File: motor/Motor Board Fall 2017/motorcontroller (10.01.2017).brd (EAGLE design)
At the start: 76.2 x 50.8 mm, 45 parts, among them CON2 MOLEX_5566-2, U1 TEENSY_3.1_BASIC_2, U2 PCA9685PW, U6 TCAN1042HVDR, X1 OSTVN02A150

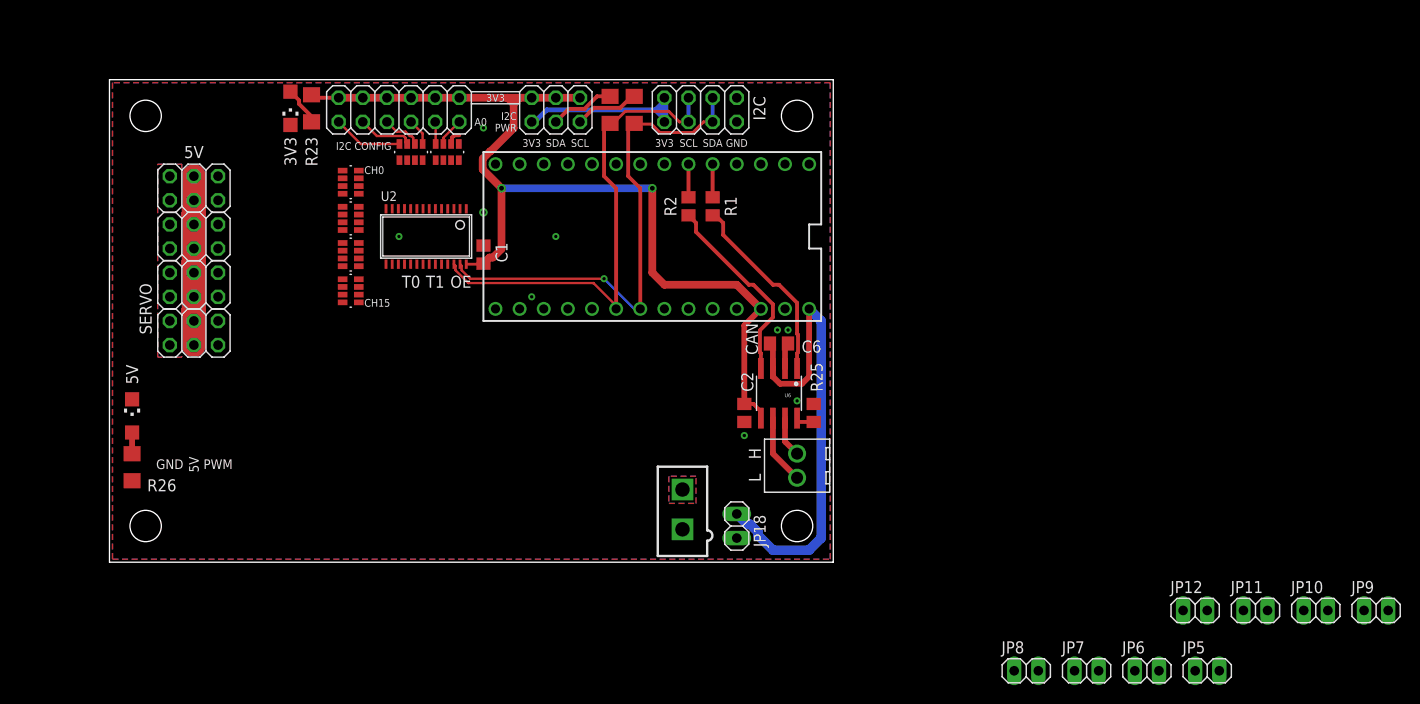
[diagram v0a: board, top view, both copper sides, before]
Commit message: Renamed labels
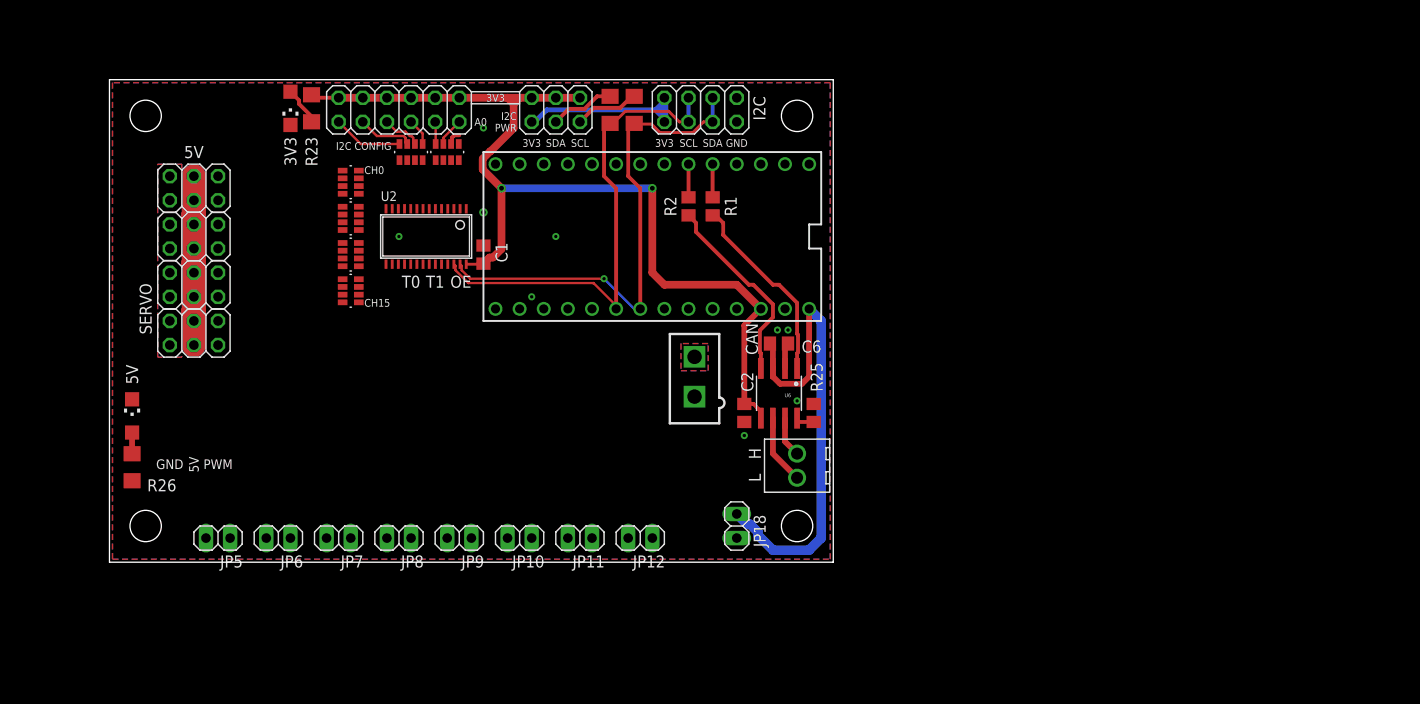
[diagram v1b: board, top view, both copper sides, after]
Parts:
- moved JP5 105.1 mm to (94.0, 74.9), turned to 180 degrees
- moved JP9 96.8 mm to (119.4, 74.9), turned to 180 degrees
- moved JP6 92.5 mm to (100.3, 74.9), turned to 180 degrees
- moved JP10 84.2 mm to (125.7, 74.9), turned to 180 degrees
- moved JP7 80.0 mm to (106.7, 74.9), turned to 180 degrees
- moved JP11 71.5 mm to (132.1, 74.9), turned to 180 degrees
- moved JP8 67.5 mm to (113.0, 74.9), turned to 180 degrees
- moved JP12 58.9 mm to (138.4, 74.9), turned to 180 degrees
- moved CON2 14.0 mm to (144.1, 91.9)
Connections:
- removed net LED_GATE0: R8.4
- removed net LED_GATE1: R8.3
- removed net LED_GATE2: R8.2
- removed net LED_GATE3: R8.1
- removed net PWM_SERVO10: R7.3
- removed net PWM_SERVO11: R7.4
- removed net PWM_SERVO8: R7.1
- removed net PWM_SERVO9: R7.2
- new net PWM_ESC0: R5.1
- new net PWM_ESC1: R5.2
- new net PWM_ESC2: R5.3
- new net PWM_ESC3: R5.4
- new net PWM_ESC4: R6.1
- new net PWM_ESC5: R6.2
- new net PWM_ESC6: R6.3
- new net PWM_ESC7: R6.4
- net PWM_SERVO0: now also R7.1; no longer R5.1
- net PWM_SERVO1: now also R7.2; no longer R5.2
- net PWM_SERVO2: now also R7.3; no longer R5.3
- net PWM_SERVO3: now also R7.4; no longer R5.4
- net PWM_SERVO4: now also R8.1; no longer R6.1
- net PWM_SERVO5: now also R8.2; no longer R6.2
- net PWM_SERVO6: now also R8.3; no longer R6.3
- net PWM_SERVO7: now also R8.4; no longer R6.4

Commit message: Rearranged board - not complete
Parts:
- moved JP12 50.7 mm to (91.4, 94.0), turned to 270 degrees
- moved JP11 47.9 mm to (91.4, 100.3), turned to 270 degrees
- moved JP9 47.2 mm to (91.4, 113.0), turned to 270 degrees
- moved JP10 46.7 mm to (91.4, 106.7), turned to 270 degrees
- moved JP6 41.0 mm to (85.1, 113.0), turned to 270 degrees
- moved JP8 33.8 mm to (85.1, 94.0), turned to 270 degrees
- moved JP7 33.3 mm to (85.1, 100.3), turned to 270 degrees
- moved JP5 33.0 mm to (85.1, 106.7), turned to 270 degrees
- moved JP21 28.4 mm to (86.4, 83.8), turned to 270 degrees
- moved JP22 22.9 mm to (91.4, 83.8), turned to 270 degrees
- moved JP23 18.5 mm to (96.5, 83.8), turned to 270 degrees
- moved R26 17.3 mm to (100.5, 74.8), turned to 0 degrees
- moved LED2 16.5 mm to (95.1, 74.8), turned to 90 degrees
- moved JP24 16.3 mm to (101.6, 83.8), turned to 270 degrees

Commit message: still working on it
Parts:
- moved JP12 53.1 mm to (141.0, 74.9), turned to 0 degrees
- moved JP11 50.1 mm to (134.6, 74.9), turned to 0 degrees
- moved JP9 48.8 mm to (121.9, 74.9), turned to 0 degrees
- moved JP10 48.6 mm to (128.3, 74.9), turned to 0 degrees
- moved JP6 42.0 mm to (102.9, 74.9), turned to 0 degrees
- moved JP8 35.9 mm to (115.6, 74.9), turned to 0 degrees
- moved JP7 35.0 mm to (109.2, 74.9), turned to 0 degrees
- moved JP5 33.7 mm to (96.5, 74.9), turned to 0 degrees
- moved JP21 28.1 mm to (88.9, 111.8), turned to 180 degrees
- moved JP22 23.0 mm to (88.9, 106.7), turned to 180 degrees
- moved JP23 19.3 mm to (88.9, 101.6), turned to 180 degrees
- moved JP24 18.0 mm to (88.9, 96.5), turned to 180 degrees
- moved R26 17.3 mm to (84.9, 82.4), turned to 270 degrees
- moved LED2 16.5 mm to (84.9, 87.8), turned to 0 degrees
- moved R8 8.28 mm to (116.2, 100.3), turned to 90 degrees
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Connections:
- removed net PWM_ESC0: R5.1
- removed net PWM_ESC1: R5.2
- removed net PWM_ESC2: R5.3
- removed net PWM_ESC3: R5.4
- removed net PWM_ESC4: R6.1
- removed net PWM_ESC5: R6.2
- removed net PWM_ESC6: R6.3
- removed net PWM_ESC7: R6.4
- net PWM_SERVO0: now also R5.1; no longer R7.1
- net PWM_SERVO1: now also R5.2; no longer R7.2
- net PWM_SERVO2: now also R5.3; no longer R7.3
- net PWM_SERVO3: now also R5.4; no longer R7.4
- net PWM_SERVO4: now also R6.1; no longer R8.1
- net PWM_SERVO5: now also R6.2; no longer R8.2
- net PWM_SERVO6: now also R6.3; no longer R8.3
- net PWM_SERVO7: now also R6.4; no longer R8.4

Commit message: not sure how to add the yellow signal lines
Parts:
- moved R7 0.64 mm to (112.4, 101.0)
- moved R8 0.64 mm to (116.2, 101.0)
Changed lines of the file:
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@@
 <setting verticaltext="up"/>
 </settings>
-<grid distance="50" unitdist="mil" unit="inch" style="dots" multiple="1" display="yes" altdistance="0.0125" altunitdist="inch" altunit="inch"/>
+<grid distance="0.025" unitdist="inch" unit="inch" style="dots" multiple="1" display="yes" altdistance="0.0125" altunitdist="inch" altunit="inch"/>
 <layers>
 <layer number="1" name="Top" color="4" fill="1" visible="yes" active="yes"/>
@@
 <text x="150.495" y="81.28" size="1.27" layer="25" rot="R90" align="center">L</text>
 <text x="150.1775" y="95.885" size="1.27" layer="25" rot="R270" align="center">CAN</text>
-<text x="93.98" y="88.9" size="1.27" layer="25" rot="R90" align="center">5V</text>
+<text x="140.97" y="90.17" size="1.27" layer="25" rot="R90" align="center">5V</text>
 <text x="84.93125" y="91.1225" size="1.27" layer="25" rot="R90" align="center-left">5V</text>
 </plain>
@@
 <attribute name="VENDOR" value="Panasonic" x="101.6" y="114.935" size="1.778" layer="27" display="off"/>
 </element>
-<element name="R7" library="ARVP" package="EXBV8V-M" value="220" x="112.395" y="100.33" smashed="yes" rot="R90">
-<attribute name="MANUFACTURER_PART_NUMBER" value="EXBV8V221JV" x="107.315" y="93.98" size="1.778" layer="27" rot="R90" display="off"/>
-<attribute name="VENDOR" value="Panasonic" x="107.315" y="93.98" size="1.778" layer="27" rot="R90" display="off"/>
-</element>
-<element name="R8" library="ARVP" package="EXBV8V-M" value="220" x="116.205" y="100.33" smashed="yes" rot="R90">
-<attribute name="MANUFACTURER_PART_NUMBER" value="EXBV8V221JV" x="106.045" y="87.63" size="1.778" layer="27" rot="R90" display="off"/>
-<attribute name="VENDOR" value="Panasonic" x="106.045" y="87.63" size="1.778" layer="27" rot="R90" display="off"/>
+<element name="R7" library="ARVP" package="EXBV8V-M" value="220" x="112.395" y="100.965" smashed="yes" rot="R90">
+<attribute name="MANUFACTURER_PART_NUMBER" value="EXBV8V221JV" x="107.315" y="94.615" size="1.778" layer="27" rot="R90" display="off"/>
+<attribute name="VENDOR" value="Panasonic" x="107.315" y="94.615" size="1.778" layer="27" rot="R90" display="off"/>
+</element>
+<element name="R8" library="ARVP" package="EXBV8V-M" value="220" x="116.205" y="100.965" smashed="yes" rot="R90">
+<attribute name="MANUFACTURER_PART_NUMBER" value="EXBV8V221JV" x="106.045" y="88.265" size="1.778" layer="27" rot="R90" display="off"/>
+<attribute name="VENDOR" value="Panasonic" x="106.045" y="88.265" size="1.778" layer="27" rot="R90" display="off"/>
 </element>
 <element name="R9" library="ARVP" package="EXBV8V-M" value="10k" x="118.11" y="115.57" smashed="yes" rot="R270">
@@
 <contactref element="U2" pad="15"/>
 <contactref element="R7" pad="8"/>
-<wire x1="111.1758" y1="101.1809" x2="111.6625" y2="103.7622" width="0" layer="19" extent="1-1"/>
+<wire x1="111.1758" y1="101.8159" x2="111.6625" y2="103.7622" width="0" layer="19" extent="1-1"/>
 </signal>
 <signal name="PWM_CH25">
 <contactref element="U2" pad="16"/>
 <contactref element="R7" pad="7"/>
-<wire x1="111.9886" y1="101.1809" x2="112.3125" y2="103.7622" width="0" layer="19" extent="1-1"/>
+<wire x1="111.9886" y1="101.8159" x2="112.3125" y2="103.7622" width="0" layer="19" extent="1-1"/>
 </signal>
 <signal name="PWM_CH26">
 <contactref element="U2" pad="17"/>
 <contactref element="R7" pad="6"/>
-<wire x1="112.8014" y1="101.1809" x2="112.9625" y2="103.7622" width="0" layer="19" extent="1-1"/>
+<wire x1="112.8014" y1="101.8159" x2="112.9625" y2="103.7622" width="0" layer="19" extent="1-1"/>
 </signal>
 <signal name="PWM_CH27">
 <contactref element="U2" pad="18"/>
 <contactref element="R7" pad="5"/>
-<wire x1="113.6142" y1="101.1809" x2="113.6125" y2="103.7622" width="0" layer="19" extent="1-1"/>
+<wire x1="113.6142" y1="101.8159" x2="113.6125" y2="103.7622" width="0" layer="19" extent="1-1"/>
 </signal>
 <signal name="PWM_CH28">
 <contactref element="U2" pad="19"/>
 <contactref element="R8" pad="8"/>
-<wire x1="114.9858" y1="101.1809" x2="114.2625" y2="103.7622" width="0" layer="19" extent="1-1"/>
+<wire x1="114.9858" y1="101.8159" x2="114.2625" y2="103.7622" width="0" layer="19" extent="1-1"/>
 </signal>
 <signal name="PWM_CH29">
 <contactref element="U2" pad="20"/>
 <contactref element="R8" pad="7"/>
-<wire x1="115.7986" y1="101.1809" x2="114.9125" y2="103.7622" width="0" layer="19" extent="1-1"/>
+<wire x1="115.7986" y1="101.8159" x2="114.9125" y2="103.7622" width="0" layer="19" extent="1-1"/>
 </signal>
 <signal name="PWM_CH30">
 <contactref element="U2" pad="21"/>
 <contactref element="R8" pad="6"/>
-<wire x1="116.6114" y1="101.1809" x2="115.5625" y2="103.7622" width="0" layer="19" extent="1-1"/>
+<wire x1="116.6114" y1="101.8159" x2="115.5625" y2="103.7622" width="0" layer="19" extent="1-1"/>
 </signal>
 <signal name="PWM_CH31">
 <contactref element="U2" pad="22"/>
 <contactref element="R8" pad="5"/>
-<wire x1="117.4242" y1="101.1809" x2="116.2125" y2="103.7622" width="0" layer="19" extent="1-1"/>
+<wire x1="117.4242" y1="101.8159" x2="116.2125" y2="103.7622" width="0" layer="19" extent="1-1"/>
 </signal>
 <signal name="A0+1">

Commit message: implemented newest design block and rearranged pcb
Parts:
- removed C6: 10u, rcl:C0805
- removed CON2: MOLEX_5566-2, ARVP:5566-2
- removed JP17: (no value), pinhead:2X03
- removed JP18: (no value), pinhead:1X02
- removed JP19: (no value), pinhead:2X04
- removed R25: 1k, rcl:R0805
- removed U$10, U$8, U$9: (no value), SparkFun:STAND-OFF
- removed U6: TCAN1042HVDR, ARVP:SOIC8
- removed X1: OSTVN02A150, dropper_torpedo_v3:OSTVN02A150
- added C5: 10u, rcl:C0805
- added CON4: MOLEX_5566-2, ARVP:5566-2
- added CON5, CON6: S3B-PH-SM4-TB, ARVP:S3B-PH-SM4-TB
- added JP13: (no value), pinhead:1X02
- added JP14: (no value), pinhead:2X04
- added JP4: (no value), pinhead:2X03
- added R11: 1k, rcl:R0805
- added U$2, U$3, U$4: (no value), SparkFun:STAND-OFF
- added U4: TCAN1042HVDR, ARVP:SO-8
- moved U$5 42.9 mm to (155.4, 119.1)
- moved C2 16.1 mm to (143.4, 103.1), turned to 180 degrees
- moved R2 9.48 mm to (136.9, 103.1), turned to 0 degrees
- moved R1 9.26 mm to (136.9, 111.0), turned to 0 degrees
- moved U1 0.57 mm to (140.2, 106.4)
- moved R3 0.57 mm to (135.8, 119.8)
- moved R4 0.57 mm to (138.3, 119.8)
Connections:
- removed net CAN_TX1: R1.2, U6.1
- removed net I2_3V1: JP17.6, JP19.7, JP19.8
- removed net TRP0: U1.16/A2
- removed net TRP1: U1.17/A3
- new net CANSH1: CON5.P$1, CON6.P$1
- new net CAN_TX2: R1.2, U4.1
- new net I2C_3V1: JP14.7, JP14.8, JP4.6
- new net PWM_ESC0: JP5.1, R7.1
- new net PWM_ESC1: JP6.1, R7.2
- new net PWM_ESC2: JP7.1, R7.3
- new net PWM_ESC3: JP8.1, R7.4
- new net PWM_ESC4: JP9.1, R8.1
- new net PWM_ESC5: JP10.1, R8.2
- new net PWM_ESC6: JP11.1, R8.3
- new net PWM_ESC7: JP12.1, R8.4
- net +3V3: now also JP4.1, JP4.3, JP4.5, U4.5; no longer JP17.1, JP17.3, JP17.5, U6.5
- net +5V: now also CON4.1, JP13.2; no longer CON2.1, JP18.2
- net CANH1: now also CON5.P$3, CON6.P$3, U4.7; no longer U6.7, X1.P$2
- net CANL1: now also CON5.P$2, CON6.P$2, U4.6; no longer U6.6, X1.P$1
- net CAN_RX1: now also U4.4; no longer U6.4
- net GND: now also C5.2, CON4.2, CON5.P$4, CON5.P$5, CON6.P$4, CON6.P$5, JP10.2, JP11.2, JP12.2, JP14.1, JP14.2, JP5.2, JP6.2, JP7.2, JP8.2, JP9.2, R11.1, U4.2; no longer C6.2, CON2.2, JP19.1, JP19.2, R25.1, U6.2
- net PCA_OE: no longer U1.11
- net SCL: now also JP14.5, JP14.6, R4.2, U1.19/A5; no longer JP19.5, JP19.6, R3.2, U1.18/A4
- net SCL_3V1: now also JP4.2; no longer JP17.2
- net SDA: now also JP14.3, JP14.4, R3.2, U1.18/A4; no longer JP19.3, JP19.4, R4.2, U1.19/A5
- net SDA_3V1: now also JP4.4; no longer JP17.4
- net STB1: now also R11.2, U4.8; no longer R25.2, U6.8
- net VIN: now also C5.1, JP13.1, U4.3; no longer C6.1, JP18.1, U6.3
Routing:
- net +3V3: track 103.9 -> 142.2 mm, vias 2 -> 4
- net CAN_TX1: track 20.4 -> 0.00 mm
- net I2C_3V1: track 0.00 -> 19.7 mm
- net I2_3V1: track 19.7 -> 0.00 mm
- net CAN_RX1: track 21.6 -> 2.46 mm
- net CAN_RX_T: track 3.49 -> 19.9 mm
- net CANH1: track 4.26 -> 16.0 mm, vias 0 -> 1
- net CANSH1: track 0.00 -> 10.9 mm, vias 0 -> 1
- net VIN: track 51.7 -> 41.2 mm, vias 0 -> 1
- net CAN_TX_T: track 3.49 -> 11.9 mm
- net +5V: track 35.6 -> 42.1 mm
- net CANL1: track 7.33 -> 13.2 mm, vias 0 -> 1
- net SDA: track 53.2 -> 57.5 mm, vias 1 -> 2
- net GND: track 4.33 -> 1.58 mm, vias 9 -> 21
- net CAN_TX2: track 0.00 -> 2.46 mm
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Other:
- board text added: "Assumptions: this board is installed in right/rear or left/front section of robot. Teensy USB connector and CAN connector should point towards the center of hull. Mounting holes come from Sparkfun library, located in projects folder. Layout can be changed if needed, as long as USB and CAN guidelines are followed."
- board text added: "Bottom"
- board text added: "S"
- board text added: "SHORT JP11 WHEN USB NOT IN USE"
- board text added: "Towards acrylic wall"
- board text added: "Towards middle of robot"
- board text removed: "5V"
- board text removed: "A0"
- board text removed: "CH0"
- board text removed: "CH15"
- board text removed: "I2C CONFIG"
- board text removed: "OE"
- board text removed: "PWM"
- board text removed: "SERVO"
- board text removed: "T0"
- board text removed: "T1"
